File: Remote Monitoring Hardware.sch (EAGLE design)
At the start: 39 parts, among them IC1 MSP430G2553, IC3 Xbee S3 Socket, IC4 MAX31855T, J5B PCC-SMP, J7 53047-06, Q1 32.768kHz

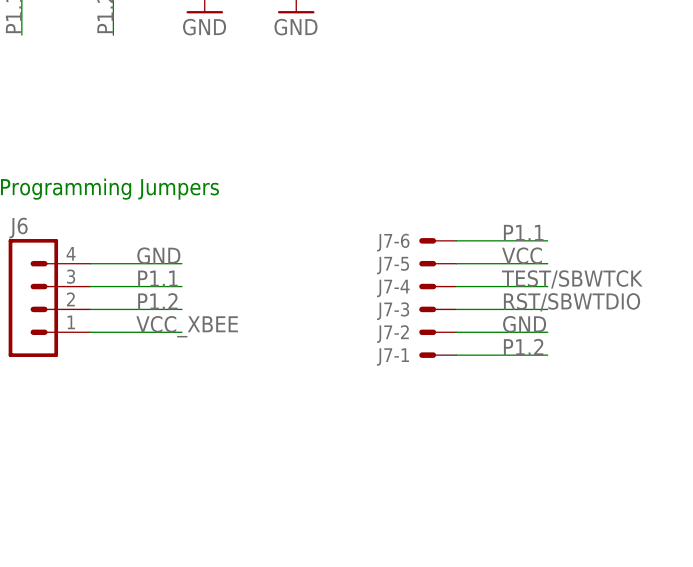
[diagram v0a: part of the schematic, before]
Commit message: larger msp430 programmer pins , new eagle project setup
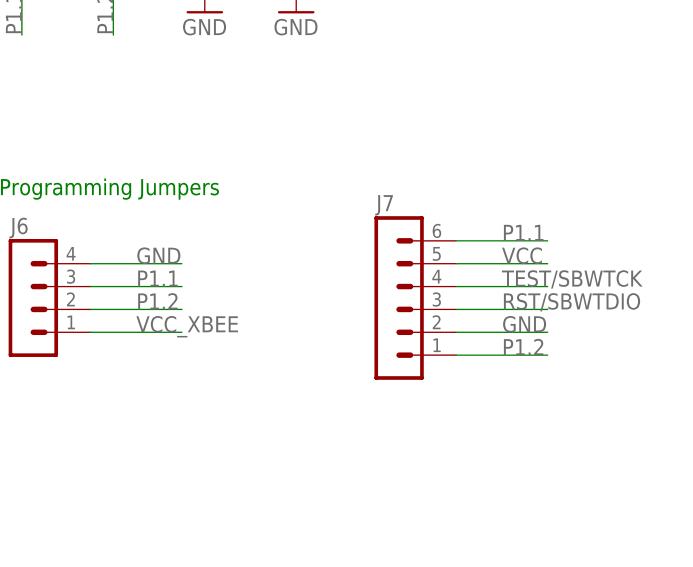
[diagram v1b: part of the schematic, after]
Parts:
- J7: value 53047-06 -> (none); device con-molex:53047-06 -> con-lstb:MA06-1
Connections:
- net GND: now also J7.2; no longer J7-2.S
- net P1.1: now also J7.6; no longer J7-6.S
- net P1.2: now also J7.1; no longer J7-1.S
- net RST/SBWTDIO: now also J7.3; no longer J7-3.S
- net TEST/SBWTCK: now also J7.4; no longer J7-4.S
- net VCC: now also J7.5; no longer J7-5.S
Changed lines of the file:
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@@
 <part name="GND19" library="supply1" deviceset="GND" device=""/>
 <part name="J6" library="con-lstb" deviceset="MA04-1" device=""/>
-<part name="J7" library="con-molex" deviceset="53?-06" device="047" value=""/>
 <part name="J4" library="SparkFun-Connectors" deviceset="CONN_02" device="3.5MM"/>
 <part name="J5A" library="SparkFun-Connectors" deviceset="CONN_02" device="3.5MM"/>
@@
 <part name="JP4" library="SparkFun-Retired" deviceset="JUMPER-2" device="PTH"/>
 <part name="JP5" library="SparkFun-Retired" deviceset="JUMPER-2" device="PTH"/>
+<part name="J7" library="con-lstb" deviceset="MA06-1" device=""/>
 </parts>
 <sheets>
@@
 <instance part="GND19" gate="1" x="220.98" y="129.54"/>
 <instance part="J6" gate="1" x="177.8" y="50.8"/>
-<instance part="J7" gate="-1" x="223.52" y="43.18" rot="R180"/>
-<instance part="J7" gate="-2" x="223.52" y="45.72" rot="R180"/>
-<instance part="J7" gate="-3" x="223.52" y="48.26" smashed="yes" rot="R180">
-<attribute name="NAME" x="220.98" y="49.022" size="1.524" layer="95" rot="R180"/>
-</instance>
-<instance part="J7" gate="-4" x="223.52" y="50.8" rot="R180"/>
-<instance part="J7" gate="-5" x="223.52" y="53.34" rot="R180"/>
-<instance part="J7" gate="-6" x="223.52" y="55.88" rot="R180"/>
 <instance part="J4" gate="G$1" x="66.04" y="157.48" smashed="yes">
 <attribute name="VALUE" x="60.96" y="152.654" size="1.778" layer="96" font="vector"/>
@@
 <instance part="JP4" gate="A" x="208.28" y="185.42"/>
 <instance part="JP5" gate="A" x="218.44" y="182.88"/>
+<instance part="J7" gate="1" x="218.44" y="50.8"/>
 </instances>
 <busses>
@@
 <wire x1="226.06" y1="45.72" x2="236.22" y2="45.72" width="0.1524" layer="91"/>
 <label x="231.14" y="45.72" size="1.778" layer="95"/>
-<pinref part="J7" gate="-2" pin="S"/>
+<pinref part="J7" gate="1" pin="2"/>
 </segment>
 <segment>
@@
 <wire x1="226.06" y1="53.34" x2="236.22" y2="53.34" width="0.1524" layer="91"/>
 <label x="231.14" y="53.34" size="1.778" layer="95"/>
-<pinref part="J7" gate="-5" pin="S"/>
+<pinref part="J7" gate="1" pin="5"/>
 </segment>
 <segment>
@@
 <wire x1="226.06" y1="43.18" x2="236.22" y2="43.18" width="0.1524" layer="91"/>
 <label x="231.14" y="43.18" size="1.778" layer="95"/>
-<pinref part="J7" gate="-1" pin="S"/>
+<pinref part="J7" gate="1" pin="1"/>
 </segment>
 <segment>
@@
 <wire x1="226.06" y1="50.8" x2="236.22" y2="50.8" width="0.1524" layer="91"/>
 <label x="231.14" y="50.8" size="1.778" layer="95"/>
-<pinref part="J7" gate="-4" pin="S"/>
+<pinref part="J7" gate="1" pin="4"/>
 </segment>
 </net>
@@
 <wire x1="226.06" y1="48.26" x2="236.22" y2="48.26" width="0.1524" layer="91"/>
 <label x="231.14" y="48.26" size="1.778" layer="95"/>
-<pinref part="J7" gate="-3" pin="S"/>
+<pinref part="J7" gate="1" pin="3"/>
 </segment>
 <segment>
@@
 <wire x1="226.06" y1="55.88" x2="236.22" y2="55.88" width="0.1524" layer="91"/>
 <label x="231.14" y="55.88" size="1.778" layer="95"/>
-<pinref part="J7" gate="-6" pin="S"/>
-</segment>
-<segment>
+<pinref part="J7" gate="1" pin="6"/>
+</segment>
+<segment>
